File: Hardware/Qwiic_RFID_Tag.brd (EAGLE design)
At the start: 30.5 x 44.5 mm, 50 parts, among them J1 Qwiic, J2 Qwiic, U1 ST25DV64KC

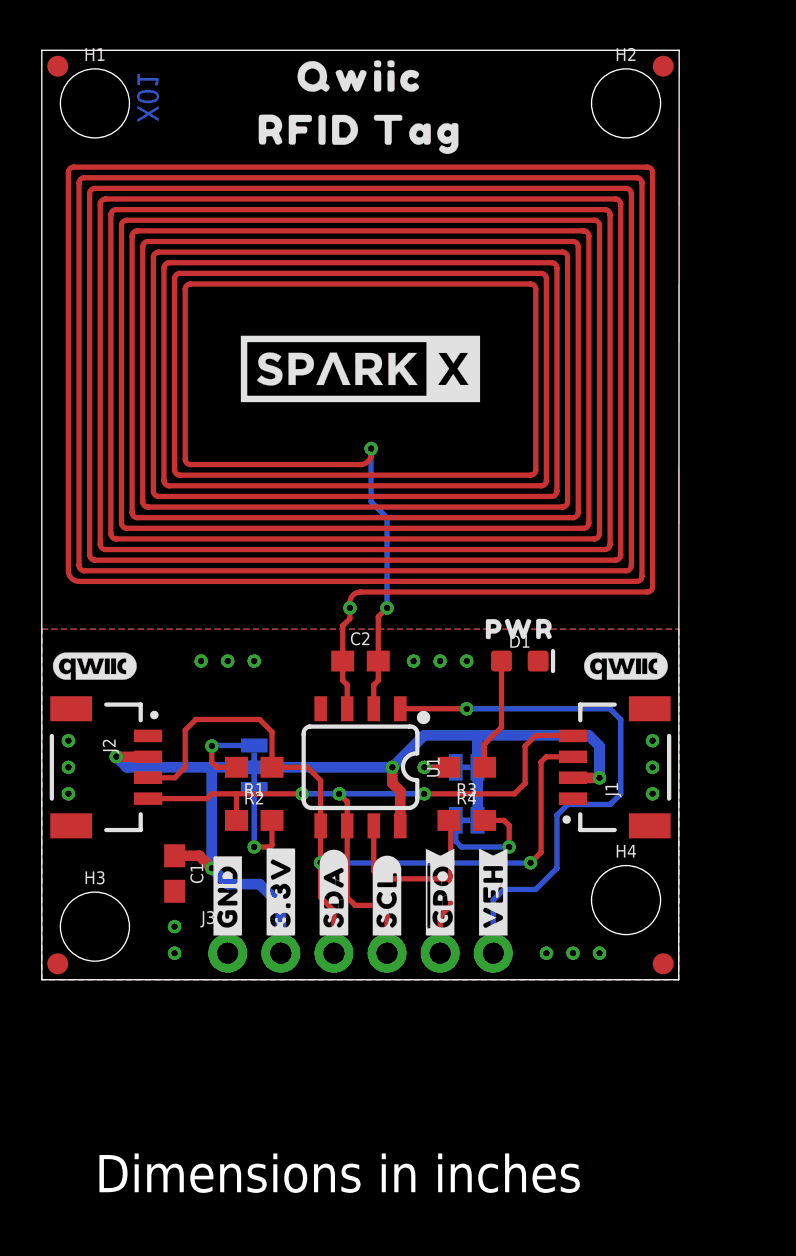
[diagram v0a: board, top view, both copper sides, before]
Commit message: Fixed misaligned mounting hole; trimmed long schematic segment.
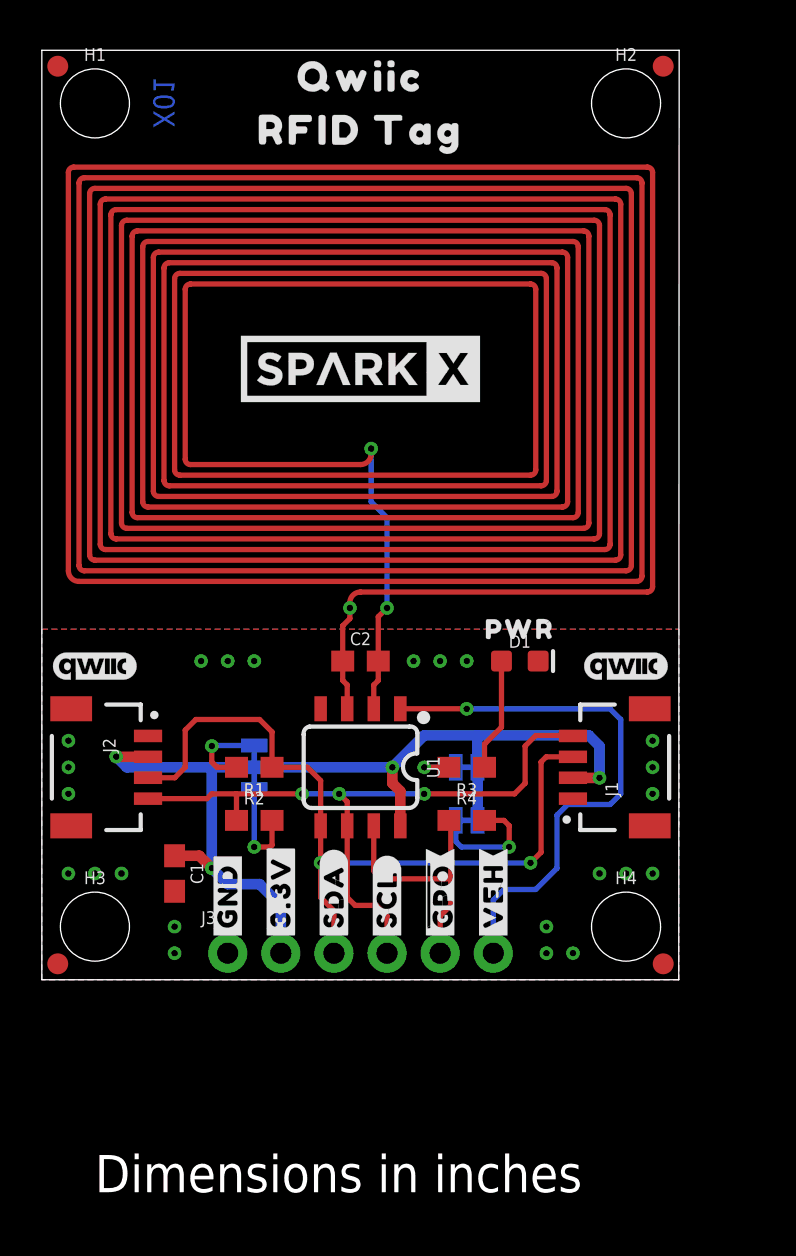
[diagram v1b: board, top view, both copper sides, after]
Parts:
- moved H4 1.27 mm to (27.9, 2.54)
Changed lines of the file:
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@@
 <drawing>
 <settings>
-<setting alwaysvectorfont="yes"/>
+<setting alwaysvectorfont="no"/>
 <setting verticaltext="up"/>
 </settings>
-<grid distance="0.01" unitdist="inch" unit="inch" style="lines" multiple="1" display="yes" altdistance="0.005" altunitdist="inch" altunit="inch"/>
+<grid distance="0.05" unitdist="inch" unit="inch" style="lines" multiple="1" display="yes" altdistance="0.005" altunitdist="inch" altunit="inch"/>
 <layers>
 <layer number="1" name="Top" color="4" fill="1" visible="yes" active="yes"/>
@@
 <dimension x1="33.02" y1="41.91" x2="33.02" y2="1.27" x3="35.56" y3="21.59" textsize="1.778" textratio="15" layer="20" dtype="vertical" unit="inch"/>
 <dimension x1="2.54" y1="46.99" x2="27.94" y2="46.99" x3="15.24" y3="48.26" textsize="1.778" textratio="15" layer="20" dtype="horizontal" unit="inch"/>
-<text x="5.588" y="43.434" size="1.016" layer="16" font="vector" ratio="15" rot="MR270">X01</text>
+<text x="6.35" y="43.18" size="1.016" layer="16" font="vector" ratio="15" rot="MR270">X01</text>
 </plain>
 <attributes>
@@
 <attribute name="VALUE" x="2.54" y="0.508" size="0.6096" layer="27" font="vector" ratio="20" align="top-center"/>
 </element>
-<element name="H4" library="SparkFun-Hardware" package="STAND-OFF" value="STAND-OFF" x="27.94" y="3.81" smashed="yes">
-<attribute name="NAME" x="27.94" y="5.842" size="0.6096" layer="25" font="vector" ratio="20" align="bottom-center"/>
-<attribute name="VALUE" x="27.94" y="1.778" size="0.6096" layer="27" font="vector" ratio="20" align="top-center"/>
+<element name="H4" library="SparkFun-Hardware" package="STAND-OFF" value="STAND-OFF" x="27.94" y="2.54" smashed="yes">
+<attribute name="NAME" x="27.94" y="4.572" size="0.6096" layer="25" font="vector" ratio="20" align="bottom-center"/>
+<attribute name="VALUE" x="27.94" y="0.508" size="0.6096" layer="27" font="vector" ratio="20" align="top-center"/>
 </element>
 <element name="U$1" library="SparkX" package="SPARKX-LARGE" value="SPARKX-LOGO5" x="15.24" y="29.21" smashed="yes"/>
@@
 <via x="24.13" y="1.27" extent="1-16" drill="0.3048"/>
 <via x="25.4" y="1.27" extent="1-16" drill="0.3048"/>
-<via x="26.67" y="1.27" extent="1-16" drill="0.3048"/>
+<via x="24.13" y="2.54" extent="1-16" drill="0.3048"/>
 <via x="29.21" y="11.43" extent="1-16" drill="0.3048"/>
 <via x="29.21" y="10.16" extent="1-16" drill="0.3048"/>
 <via x="29.21" y="8.89" extent="1-16" drill="0.3048"/>
+<via x="26.67" y="5.08" extent="1-16" drill="0.3048"/>
+<via x="29.21" y="5.08" extent="1-16" drill="0.3048"/>
+<via x="27.94" y="5.08" extent="1-16" drill="0.3048"/>
+<via x="1.27" y="5.08" extent="1-16" drill="0.3048"/>
+<via x="3.81" y="5.08" extent="1-16" drill="0.3048"/>
+<via x="2.54" y="5.08" extent="1-16" drill="0.3048"/>
 </signal>
 <signal name="3.3V">
